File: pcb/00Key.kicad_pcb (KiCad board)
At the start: 2 copper layers, 255 parts, among them Q1 IRLZ44N, U1 Teensy4.1

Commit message: diodes layout
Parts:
- moved OLED1 648.8 mm to (379.4, 47.3)
- moved D_RBRAC_1 425.4 mm to (267.7, 75.9), turned to 270 degrees
- moved D_HOME_1 391.6 mm to (293.1, 75.9), turned to 270 degrees
- moved D_DELETE_1 387.4 mm to (290.5, 77.8), turned to 270 degrees
- moved D_END_1 371.4 mm to (300.7, 70.2), turned to 270 degrees
- moved D_FN_1 366.4 mm to (249.9, 68.3), turned to 270 degrees
- moved D_ENTER_1 358.5 mm to (270.2, 74.0), turned to 270 degrees
- moved D_PRTSC_1 353.4 mm to (265.1, 77.8), turned to 270 degrees
- moved D_DOWN_1 350.2 mm to (288.0, 70.2), turned to 270 degrees
- moved D_RIGHT_1 340.9 mm to (303.2, 68.3), turned to 270 degrees
- moved D_PGUP_1 338.9 mm to (295.6, 74.0), turned to 270 degrees
- moved D_DOT_1 338.1 mm to (232.1, 70.2), turned to 270 degrees
- moved D_UP_1 326.7 mm to (285.4, 72.1), turned to 270 degrees
- moved D_0_1 323.1 mm to (224.5, 75.9), turned to 270 degrees
- moved D_PGDN_1 317.4 mm to (298.1, 72.1), turned to 270 degrees
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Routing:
- net col13: track 0.00 -> 122.7 mm
- net col3: track 0.00 -> 105.8 mm
- net col11: track 0.00 -> 103.5 mm
- net col10: track 0.00 -> 103.4 mm
- net col1: track 0.00 -> 103.2 mm
- net col12: track 0.00 -> 102.9 mm
- net col6: track 0.00 -> 101.0 mm
- net col14: track 0.00 -> 99.1 mm
- net col0: track 0.00 -> 95.4 mm
- net col15: track 0.00 -> 91.6 mm
- net col2: track 0.00 -> 84.4 mm
- net col8: track 0.00 -> 82.2 mm
- net col7: track 0.00 -> 82.2 mm
- net col5: track 0.00 -> 82.0 mm
- net col9: track 0.00 -> 81.4 mm
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
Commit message: start resistor placement
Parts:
- moved Q1 464.4 mm to (188.1, 284.5)
- moved R1 464.4 mm to (155.3, 273.9)
- moved R2 464.4 mm to (155.3, 269.9)
- moved R_2_1 464.4 mm to (123.0, 273.9)
- moved R_3_1 464.4 mm to (176.9, 265.8)
- moved R_4_1 464.4 mm to (166.1, 269.9)
- moved R_5_1 464.4 mm to (166.1, 273.9)
- moved R_6_1 464.4 mm to (176.9, 269.9)
- moved R_8_1 464.4 mm to (187.7, 265.8)
- moved R_9_1 464.4 mm to (187.7, 269.9)
- moved R_A_1 464.4 mm to (187.7, 273.9)
- moved R_BKSPACE_1 464.4 mm to (198.4, 269.9)
- moved R_BSLSH_1 464.4 mm to (198.4, 273.9)
- moved R_B_1 464.4 mm to (198.4, 265.8)
- moved R_COMMA_1 464.4 mm to (209.2, 273.9)
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
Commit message: first layout
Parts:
- removed R1: 470, Resistor_THT:R_Axial_DIN0207_L6.3mm_D2.5mm_P7.62mm_Horizontal
- added R_Z_1: 470, Resistor_THT:R_Axial_DIN0207_L6.3mm_D2.5mm_P7.62mm_Horizontal, F.Cu at (115.8, 77.1)
- moved R_RIGHT_1 266.4 mm to (315.8, 75.2), turned to 90 degrees
- moved R_HOME_1 253.2 mm to (304.4, 82.8), turned to 90 degrees
- moved R_LEFT_1 248.3 mm to (284.4, 77.1), turned to 90 degrees
- moved Q1 244.2 mm to (323.0, 81.0)
- moved R_PGDN_1 243.0 mm to (310.1, 79.0), turned to 90 degrees
- moved R_W_1 227.7 mm to (124.3, 80.9), turned to 90 degrees
- moved R_DELETE_1 226.1 mm to (301.5, 84.7), turned to 90 degrees
- moved R_X_1 225.7 mm to (130.0, 77.1), turned to 90 degrees
- moved R_LBRAC_1 220.3 mm to (264.4, 80.9), turned to 90 degrees
- moved R_BSLSH_1 214.9 mm to (292.9, 80.9), turned to 90 degrees
- moved R_I_1 210.5 mm to (215.8, 80.9), turned to 90 degrees
- moved R_MINUS_1 210.4 mm to (244.3, 82.8), turned to 90 degrees
- moved R_L_1 210.3 mm to (232.9, 79.0), turned to 90 degrees
- moved R_A_1 208.8 mm to (112.9, 79.0), turned to 90 degrees
- moved R_K_1 208.5 mm to (218.6, 79.0), turned to 90 degrees
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- renumbered R2 to R_F6_1

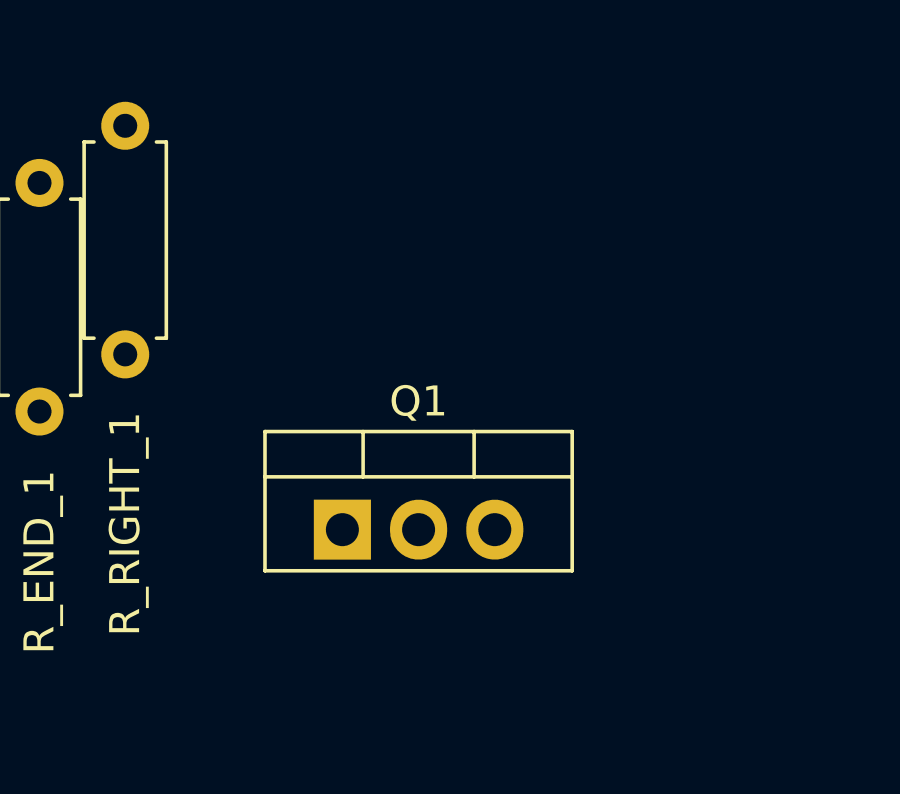
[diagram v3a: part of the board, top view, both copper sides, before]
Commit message: pulldown resistor mosfet
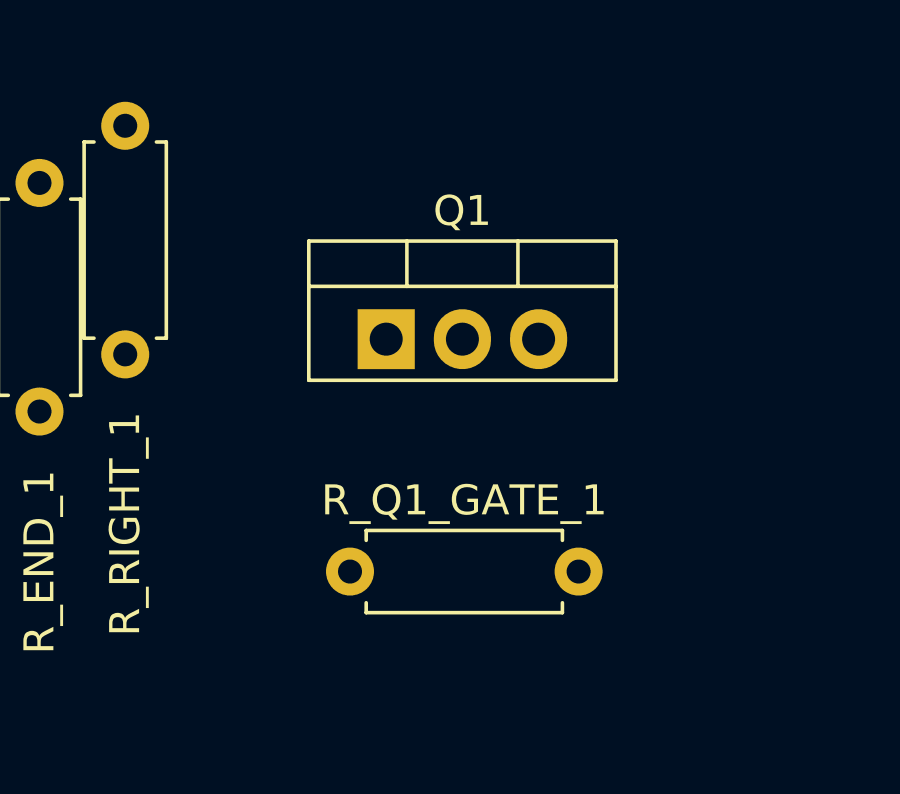
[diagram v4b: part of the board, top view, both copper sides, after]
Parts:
- added R_Q1_GATE_1: 10K, Resistor_THT:R_Axial_DIN0207_L6.3mm_D2.5mm_P7.62mm_Horizontal, F.Cu at (323.3, 82.4)
- moved Q1 6.52 mm to (324.5, 74.7)

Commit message: switches upside down
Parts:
- turned MX_0_1 to 180 degrees
- turned MX_1_1 to 180 degrees
- turned MX_2_1 to 180 degrees
- turned MX_3_1 to 180 degrees
- turned MX_4_1 to 180 degrees
- turned MX_5_1 to 180 degrees
- turned MX_6_1 to 180 degrees
- turned MX_7_1 to 180 degrees
- turned MX_8_1 to 180 degrees
- turned MX_9_1 to 180 degrees
- turned MX_A_1 to 180 degrees
- turned MX_BKSPACE_1 to 180 degrees
- turned MX_BSLSH_1 to 180 degrees
- turned MX_B_1 to 180 degrees
- turned MX_CAPS_1 to 180 degrees
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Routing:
- net col13: track 122.7 -> 0.00 mm
- net col3: track 105.8 -> 0.00 mm
- net col11: track 103.5 -> 0.00 mm
- net col10: track 103.4 -> 0.00 mm
- net col1: track 103.2 -> 0.00 mm
- net col12: track 102.9 -> 0.00 mm
- net col6: track 101.0 -> 0.00 mm
- net col14: track 99.1 -> 0.00 mm
- net col0: track 95.4 -> 0.00 mm
- net col15: track 91.6 -> 0.00 mm
- net col2: track 84.4 -> 0.00 mm
- net col8: track 82.2 -> 0.00 mm
- net col7: track 82.2 -> 0.00 mm
- net col5: track 82.0 -> 0.00 mm
- net col9: track 81.4 -> 0.00 mm
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
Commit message: reversed stabs
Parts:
- MX_BKSPACE_1: footprint keys:MX-2U -> keys:MX-2U-ReversedStabilizers
- MX_ENTER_1, MX_LSHIFT_1: footprint keys:MX-2.25U -> keys:MX-2.25U-ReversedStabilizers
- MX_SPACE_1: footprint keys:MX-6.25U -> keys:MX-6.25U-ReversedStabilizers

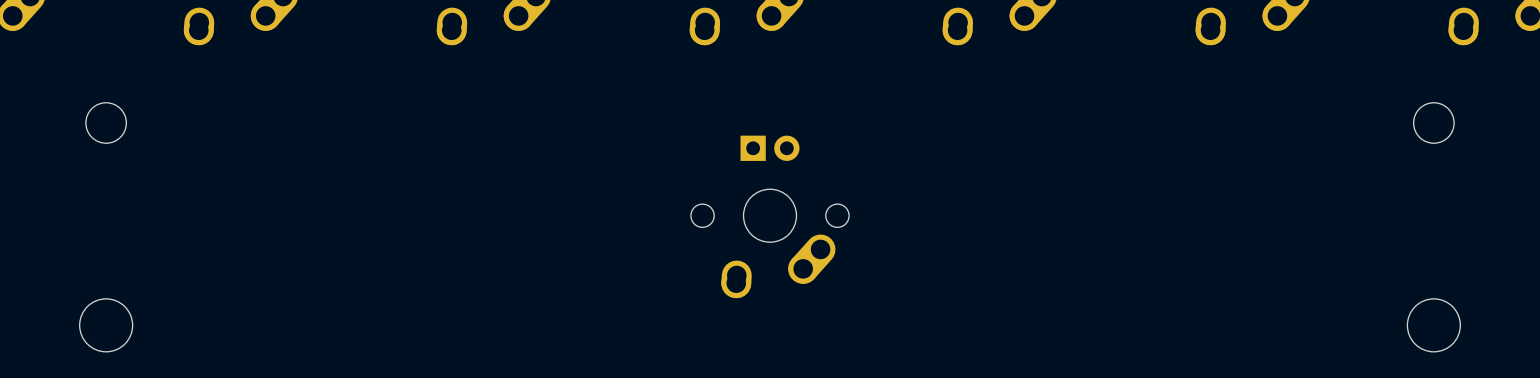
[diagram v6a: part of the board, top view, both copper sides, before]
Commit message: reversed space stab
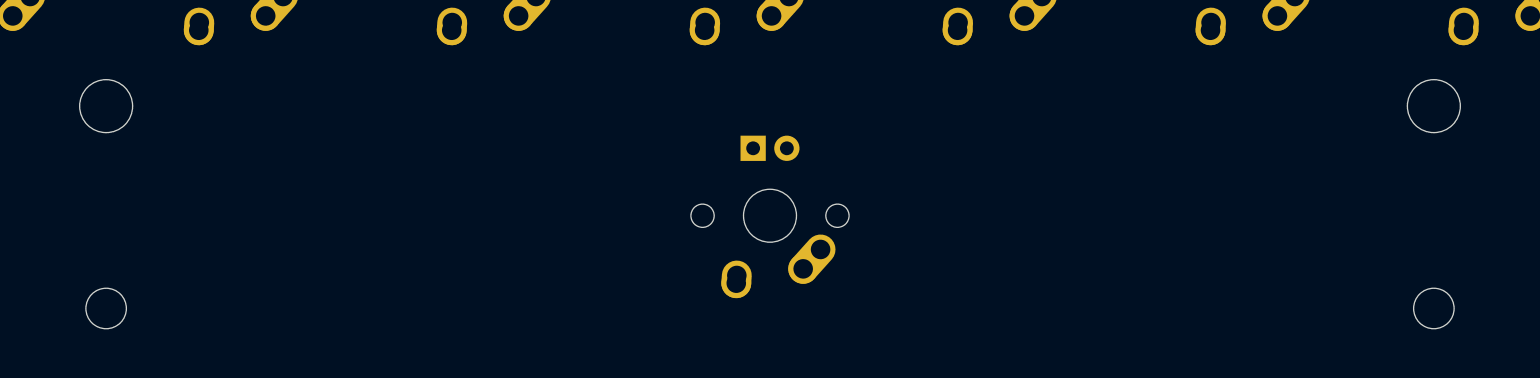
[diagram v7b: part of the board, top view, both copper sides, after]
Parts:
- MX_SPACE_1: footprint keys:MX-6.25U-ReversedStabilizers -> keys:MX-6.25U

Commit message: edge cuts, first mouthing holes
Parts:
- added REF**: MountingHole_2.2mm_M2_Pad, MountingHole:MountingHole_2.2mm_M2_Pad, F.Cu at (340.7, 93.0)
- added REF**: MountingHole_2.2mm_M2_Pad, MountingHole:MountingHole_2.2mm_M2_Pad, F.Cu at (340.7, 41.6)
- added REF**: MountingHole_2.2mm_M2_Pad, MountingHole:MountingHole_2.2mm_M2_Pad, F.Cu at (43.5, 93.0)
- added REF**: MountingHole_2.2mm_M2_Pad, MountingHole:MountingHole_2.2mm_M2_Pad, F.Cu at (43.5, 41.6)
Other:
- board outline added: 304.8 x 173.4 mm
